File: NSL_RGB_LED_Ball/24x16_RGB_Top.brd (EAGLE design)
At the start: 44 x 44 mm, 16 parts

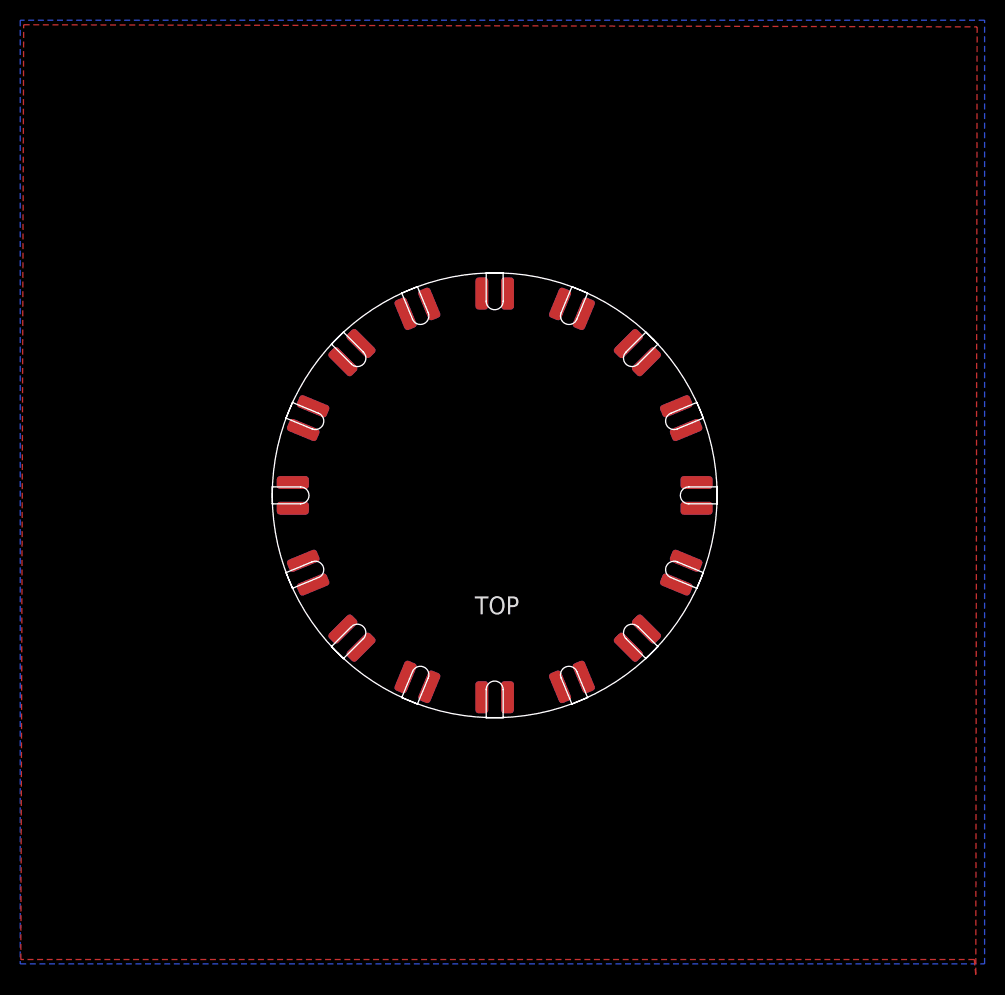
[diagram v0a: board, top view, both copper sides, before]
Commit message: 
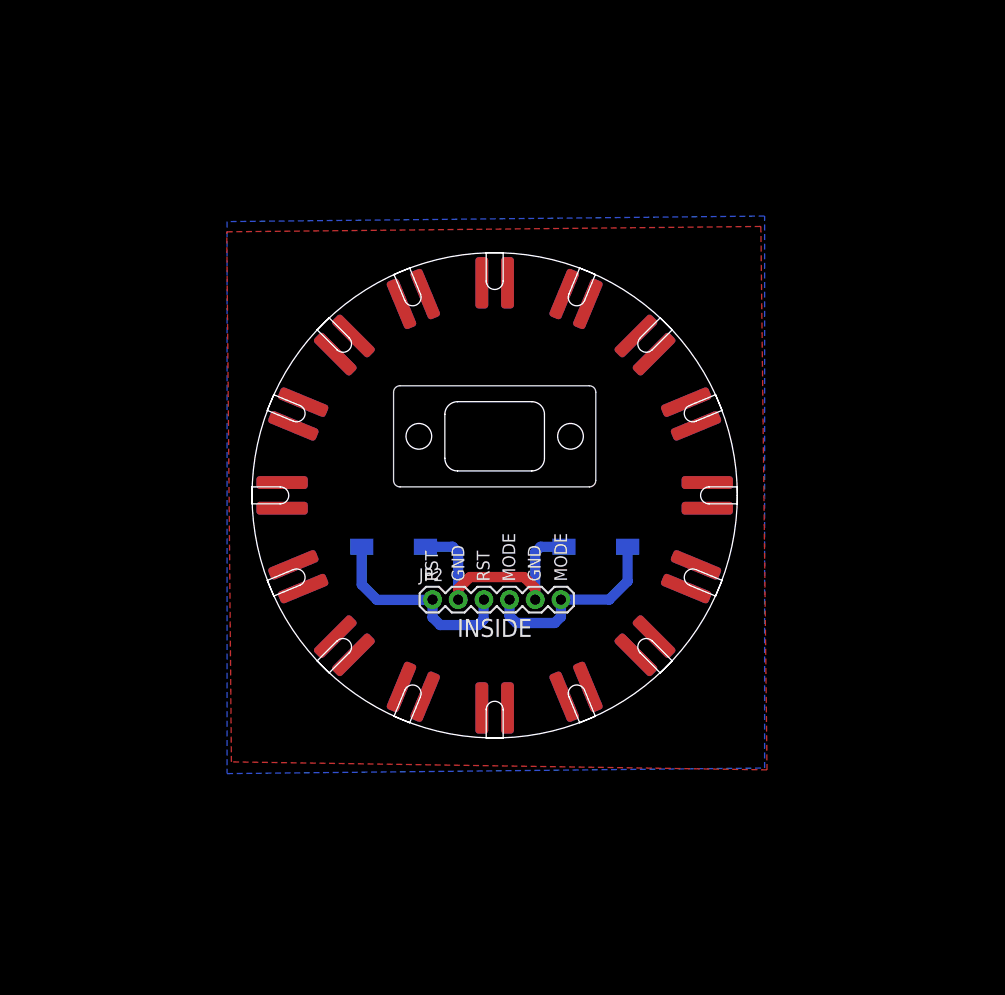
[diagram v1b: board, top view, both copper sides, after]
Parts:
- added JP2: (no value), SparkFun-Connectors:1X06
- added S1, S2: SPARKFUN-ELECTROMECHANICAL_SWITCH-MOMENTARY-2-SMD-1101NE, tvbgone-2layer:SPARKFUN-ELECTROMECHANICAL_TACTILE-SWITCH-1101NE
- added U$1: USB_PANNEL, 24x16_RGB_Bottom:USB_PANNEL
- SLOT1, SLOT10, SLOT11, SLOT12, SLOT13, SLOT14, SLOT15, SLOT16, SLOT2, SLOT3, SLOT4, SLOT5, SLOT6, SLOT7, SLOT8, SLOT9: device slice:SLOT -> 24x16_RGB_Bottom:SLOT
- moved SLOT10 2.00 mm to (-22.2, -9.18)
- moved SLOT12 2.00 mm to (-9.18, -22.2)
- moved SLOT14 2.00 mm to (9.18, -22.2)
- moved SLOT16 2.00 mm to (22.2, -9.18)
- moved SLOT2 2.00 mm to (22.2, 9.18)
- moved SLOT4 2.00 mm to (9.18, 22.2)
- moved SLOT6 2.00 mm to (-9.18, 22.2)
- moved SLOT8 2.00 mm to (-22.2, 9.18)
- moved SLOT1 2.00 mm to (24.0, 0.00)
- moved SLOT13 2.00 mm to (0.00, -24.0)
- moved SLOT5 2.00 mm to (0.00, 24.0)
- moved SLOT9 2.00 mm to (-24.0, 0.00)
- moved SLOT11 2.00 mm to (-17.0, -17.0)
- moved SLOT15 2.00 mm to (17.0, -17.0)
- moved SLOT3 2.00 mm to (17.0, 17.0)
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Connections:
- new net MODE: JP2.4, JP2.6, S1.P$1
- new net RST: JP2.1, JP2.3, S2.P$1
- net BLANK: now also SLOT1.P$1, SLOT1.P$2, SLOT10.P$1, SLOT10.P$2, SLOT11.P$1, SLOT11.P$2, SLOT12.P$1, SLOT12.P$2, SLOT13.P$1, SLOT13.P$2, SLOT14.P$1, SLOT14.P$2, SLOT15.P$1, SLOT15.P$2, SLOT16.P$1, SLOT16.P$2, SLOT2.P$1, SLOT2.P$2, SLOT3.P$1, SLOT3.P$2, SLOT4.P$1, SLOT4.P$2, SLOT5.P$1, SLOT5.P$2, SLOT6.P$1, SLOT6.P$2, SLOT7.P$1, SLOT7.P$2, SLOT8.P$1, SLOT8.P$2, SLOT9.P$1, SLOT9.P$2; no longer SLOT1.P$3, SLOT1.P$4, SLOT10.P$3, SLOT10.P$4, SLOT11.P$3, SLOT11.P$4, SLOT12.P$3, SLOT12.P$4, SLOT13.P$3, SLOT13.P$4, SLOT14.P$3, SLOT14.P$4, SLOT15.P$3, SLOT15.P$4, SLOT16.P$3, SLOT16.P$4, SLOT2.P$3, SLOT2.P$4, SLOT3.P$3, SLOT3.P$4, SLOT4.P$3, SLOT4.P$4, SLOT5.P$3, SLOT5.P$4, SLOT6.P$3, SLOT6.P$4, SLOT7.P$3, SLOT7.P$4, SLOT8.P$3, SLOT8.P$4, SLOT9.P$3, SLOT9.P$4
- net GND: now also JP2.2, JP2.5, S1.P$2, S2.P$2, SLOT1.P$3, SLOT1.P$4, SLOT10.P$3, SLOT10.P$4, SLOT11.P$3, SLOT11.P$4, SLOT12.P$3, SLOT12.P$4, SLOT13.P$3, SLOT13.P$4, SLOT14.P$3, SLOT14.P$4, SLOT15.P$3, SLOT15.P$4, SLOT16.P$3, SLOT16.P$4, SLOT2.P$3, SLOT2.P$4, SLOT3.P$3, SLOT3.P$4, SLOT4.P$3, SLOT4.P$4, SLOT5.P$3, SLOT5.P$4, SLOT6.P$3, SLOT6.P$4, SLOT7.P$3, SLOT7.P$4, SLOT8.P$3, SLOT8.P$4, SLOT9.P$3, SLOT9.P$4; no longer SLOT1.P$1, SLOT1.P$2, SLOT10.P$1, SLOT10.P$2, SLOT11.P$1, SLOT11.P$2, SLOT12.P$1, SLOT12.P$2, SLOT13.P$1, SLOT13.P$2, SLOT14.P$1, SLOT14.P$2, SLOT15.P$1, SLOT15.P$2, SLOT16.P$1, SLOT16.P$2, SLOT2.P$1, SLOT2.P$2, SLOT3.P$1, SLOT3.P$2, SLOT4.P$1, SLOT4.P$2, SLOT5.P$1, SLOT5.P$2, SLOT6.P$1, SLOT6.P$2, SLOT7.P$1, SLOT7.P$2, SLOT8.P$1, SLOT8.P$2, SLOT9.P$1, SLOT9.P$2
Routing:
- net GND: track 0.00 -> 26.7 mm
- net RST: track 0.00 -> 20.7 mm
- net MODE: track 0.00 -> 19.7 mm
- added copper zone on layer 1, net BLANK
- added copper zone on layer 16, net GND
- removed copper zone on layer 16, net BLANK
- removed copper zone on layer 1, net GND
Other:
- board size 44 x 44 mm -> 48 x 48 mm
- board text added: "A"
- board text added: "GND"
- board text added: "MODE"
- board text added: "Mode"
- board text added: "RST"
- board text added: "Reset"
- board text added: "nullspacelabs.com"
- board text removed: "TOP"

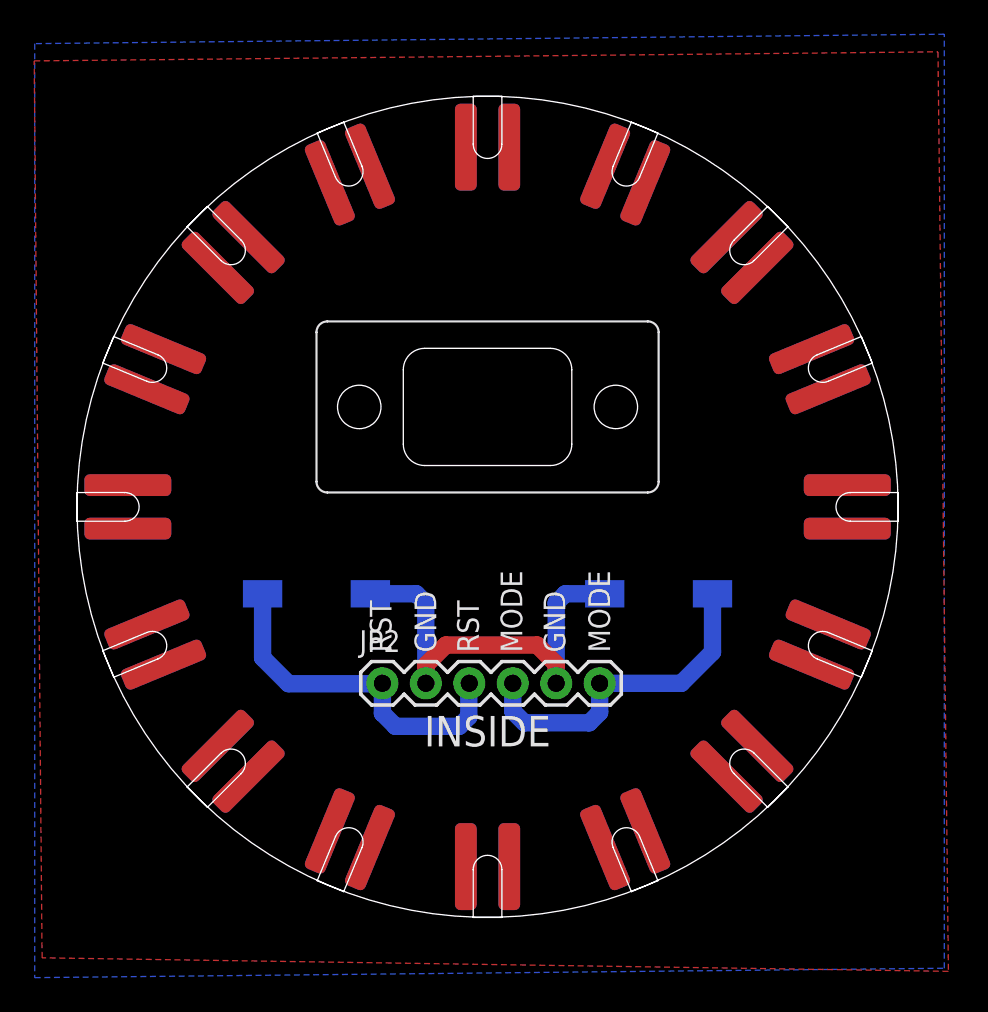
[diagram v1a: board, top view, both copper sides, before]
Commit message: 
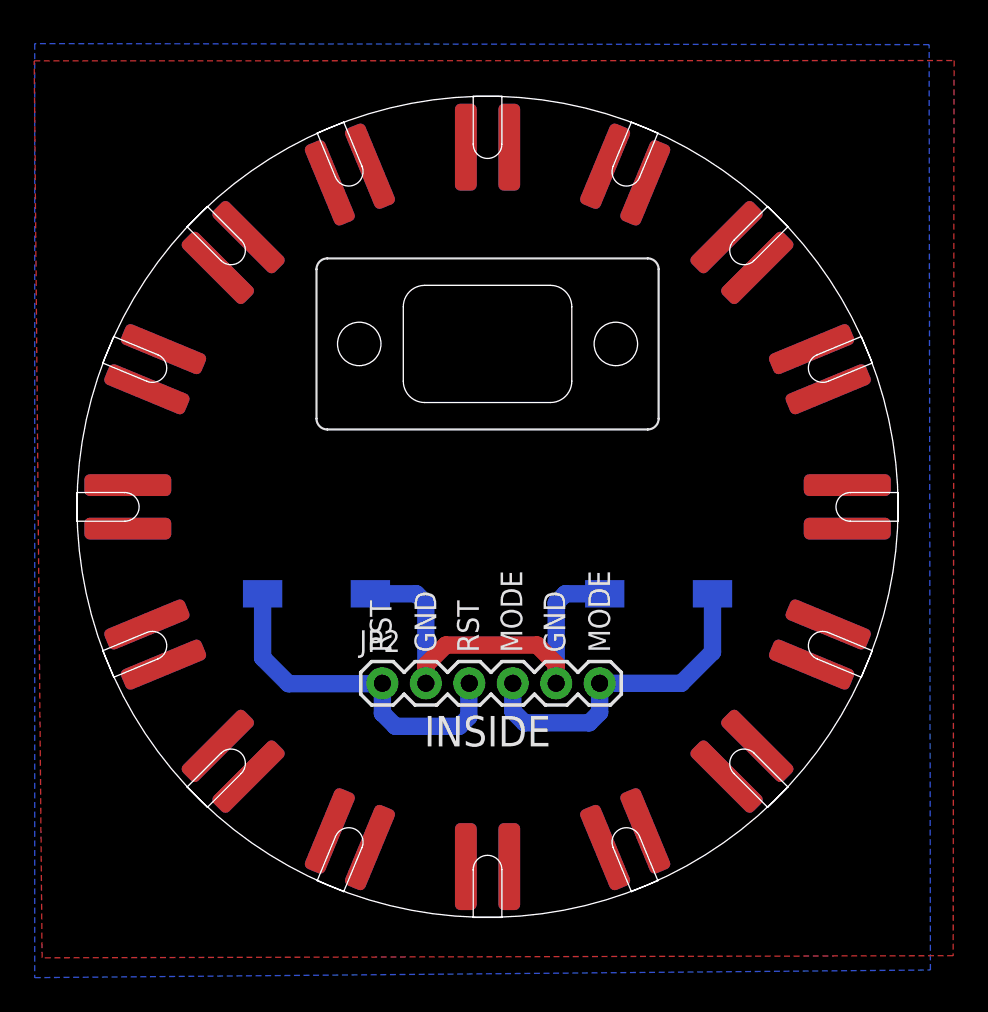
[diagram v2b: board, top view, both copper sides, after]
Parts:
- moved U$1 3.68 mm to (0.00, 9.53)
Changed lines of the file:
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@@
 <layer number="44" name="Drills" color="7" fill="1" visible="no" active="yes"/>
 <layer number="45" name="Holes" color="7" fill="1" visible="no" active="yes"/>
-<layer number="46" name="Milling" color="3" fill="1" visible="no" active="yes"/>
+<layer number="46" name="Milling" color="3" fill="1" visible="yes" active="yes"/>
 <layer number="47" name="Measures" color="7" fill="1" visible="no" active="yes"/>
 <layer number="48" name="Document" color="7" fill="1" visible="no" active="yes"/>
@@
 <text x="7.1628" y="-8.509" size="1.27" layer="21" font="vector" rot="R90">MODE</text>
 <text x="-0.508" y="-8.509" size="1.27" layer="21" font="vector" rot="R90">RST</text>
-<text x="0" y="-1.4732" size="2.032" layer="22" font="vector" rot="MR0" align="center">nullspacelabs.com</text>
+<text x="0" y="0" size="2.032" layer="22" font="vector" rot="MR0" align="center">nullspacelabs.com</text>
 </plain>
 <attributes>
@@
 <element name="S2" library="tvbgone-2layer" package="SPARKFUN-ELECTROMECHANICAL_TACTILE-SWITCH-1101NE" value="SPARKFUN-ELECTROMECHANICAL_SWITCH-MOMENTARY-2-SMD-1101NE" x="-10" y="-5.08" rot="MR180"/>
 <element name="JP2" library="SparkFun-Connectors" package="1X06" value="" x="-6.1468" y="-10.3124"/>
-<element name="U$1" library="24x16_RGB_Bottom" package="USB_PANNEL" value="USB_PANNEL" x="0" y="5.842"/>
+<element name="U$1" library="24x16_RGB_Bottom" package="USB_PANNEL" value="USB_PANNEL" x="0" y="9.525"/>
 </elements>
 <signals>
@@
 <vertex x="-26.47" y="27.08"/>
 <vertex x="-26.47" y="-27.52"/>
-<vertex x="26.7" y="-26.97"/>
-<vertex x="26.7" y="27.63"/>
+<vertex x="25.8872" y="-27.0716"/>
+<vertex x="25.811" y="27.0204"/>
 </polygon>
 </signal>
@@
 <contactref element="SLOT16" pad="P$2"/>
 <polygon width="0.254" layer="1">
-<vertex x="26.33" y="26.6"/>
-<vertex x="26.94" y="-27.15"/>
+<vertex x="27.2698" y="26.092"/>
+<vertex x="27.2194" y="-26.2356"/>
 <vertex x="-26.04" y="-26.36"/>
 <vertex x="-26.5" y="26.07"/>
